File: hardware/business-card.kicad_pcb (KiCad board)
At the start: 2 copper layers, 55.5 x 89.5 mm, 91 parts, among them J1 Connector, USB-TYPE-C-16P, U1 MAX7219EWG+T, U2 AMS1117, U3 ESP32-C3FH4, X1 40MHz, 15pF

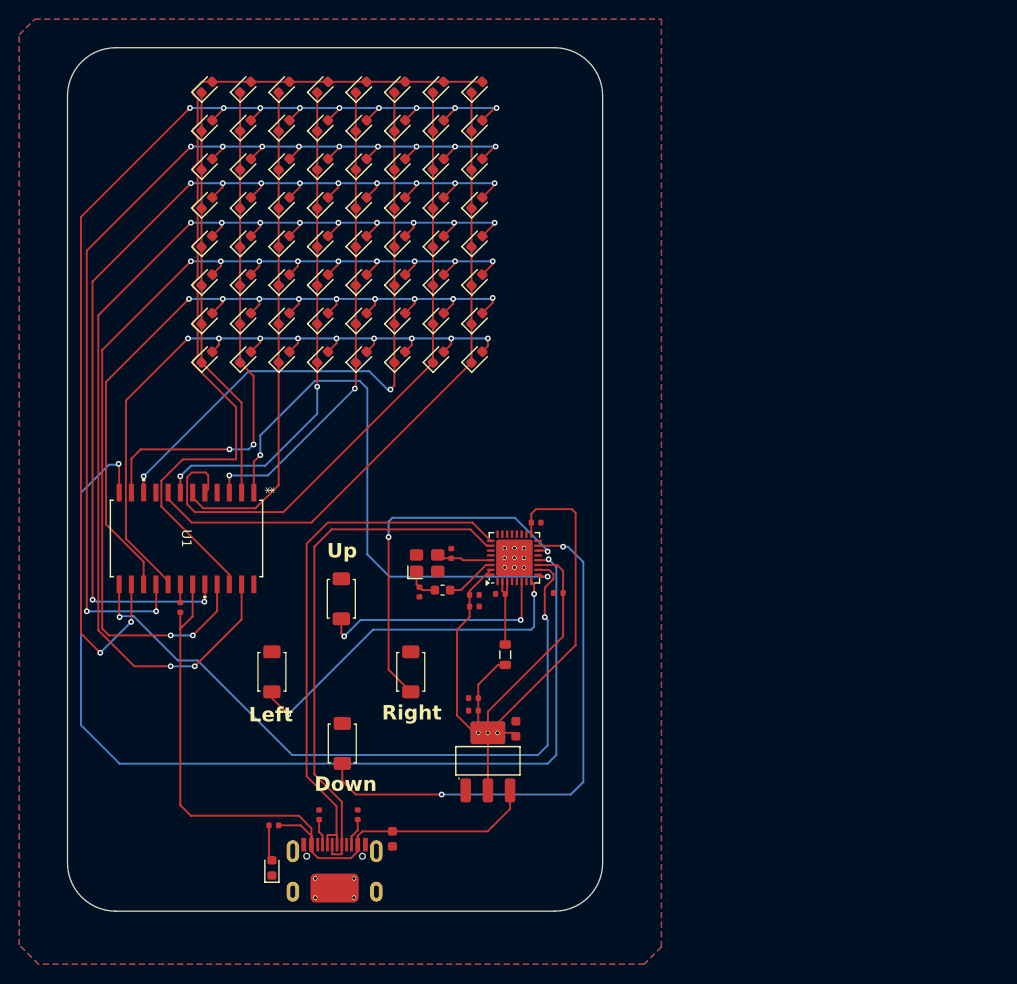
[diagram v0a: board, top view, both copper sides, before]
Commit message: Add Kicad project to hardware
Updated the hardware directory to hold the entire kicad project. Now the
pcb can be developed on multiple kicad instances and maintained in git.
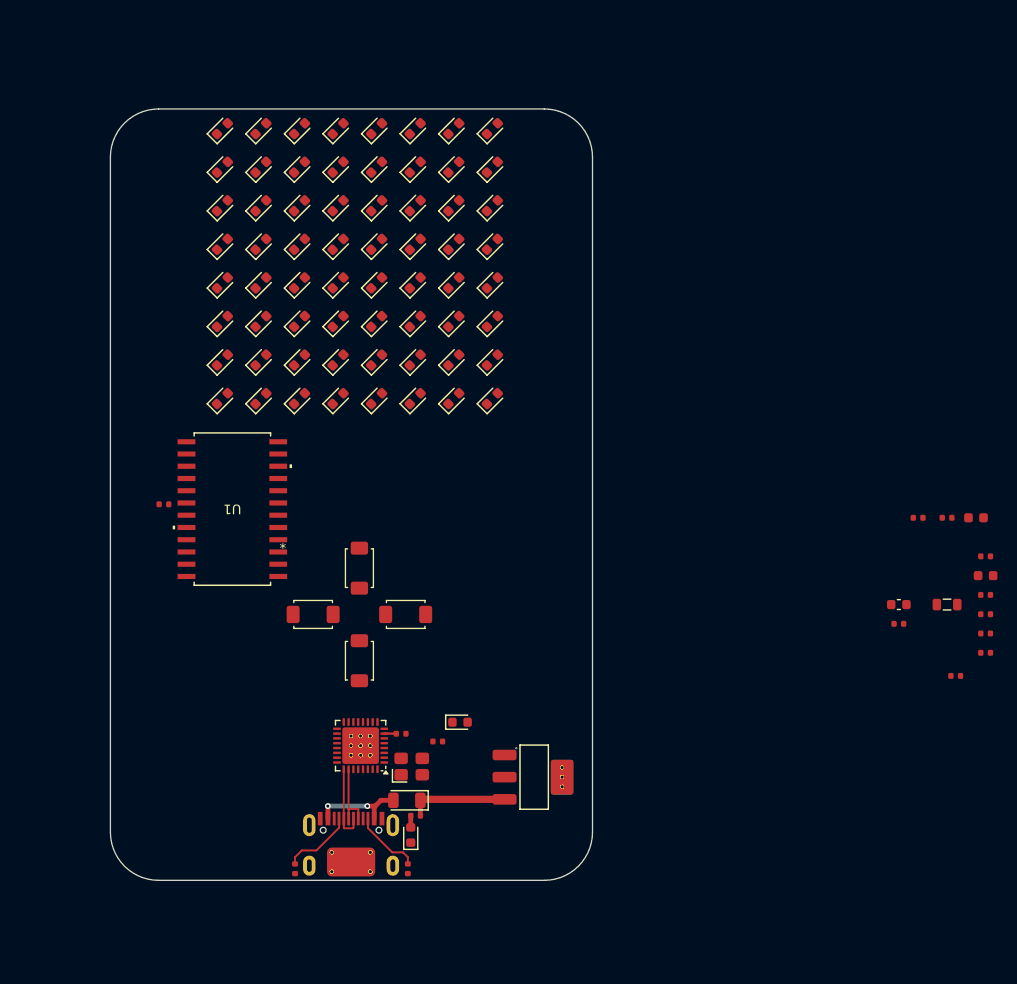
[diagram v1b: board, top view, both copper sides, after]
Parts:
- added D66: Yellow, PCM_JLCPCB:D_0603, F.Cu at (156.6, 114.4)
- added D67: SMF6.5A, PCM_JLCPCB:D_SOD-123FL, F.Cu at (151.1, 122.5)
- added R5: 1kΩ, PCM_JLCPCB:R_0402, F.Cu at (154.3, 116.4)
- added R6: 10kΩ, PCM_JLCPCB:R_0402, F.Cu at (150.5, 115.6)
- moved C1 69.1 mm to (210.1, 93.2), turned to 0 degrees
- moved C7 54.2 mm to (211.1, 101.2), turned to 0 degrees
- moved C10 53.8 mm to (208.0, 109.6), turned to 0 degrees
- moved C9 53.2 mm to (211.1, 105.2)
- moved C6 53.0 mm to (207.1, 93.2), turned to 0 degrees
- moved C4 53.0 mm to (211.1, 103.2)
- moved C2 51.2 mm to (211.1, 99.2), turned to 0 degrees
- moved C8 50.5 mm to (211.1, 97.2), turned to 0 degrees
- moved C11 49.8 mm to (202.1, 104.2), turned to 0 degrees
- moved C3 48.5 mm to (211.1, 107.2)
- moved L2 47.3 mm to (202.1, 102.2), turned to 0 degrees
- moved L1 46.1 mm to (207.1, 102.2), turned to 0 degrees
- moved C5 38.1 mm to (204.1, 93.2), turned to 0 degrees
- moved U3 25.2 mm to (146.3, 116.8), turned to 180 degrees
- moved X1 21.2 mm to (151.6, 119.0)
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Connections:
- J1 pad A9B4: VBUS -> Net-(D67-Pad2)
- J1 pad B9A4: VBUS -> Net-(D67-Pad2)
- R2 pad 2: Net-(R2-Pad2) -> GND
- U3 pad 7: unconnected-(U3-CHIP_EN-Pad7) -> Net-(U3-CHIP_EN)
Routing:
- net /R2: track 116.7 -> 0.00 mm, vias 11 -> 0
- net /R5: track 114.6 -> 0.00 mm, vias 11 -> 0
- net /R3: track 108.8 -> 0.00 mm, vias 11 -> 0
- net /R4: track 108.3 -> 0.00 mm, vias 11 -> 0
- net /GPIO6: track 105.4 -> 0.00 mm, vias 2 -> 0
- net /R6: track 103.6 -> 0.00 mm, vias 11 -> 0
- net /R1: track 95.5 -> 0.00 mm
- net +3.3V: track 95.2 -> 0.00 mm
- net /R7: track 81.5 -> 0.00 mm, vias 9 -> 0
- net /R8: track 75.0 -> 0.00 mm, vias 9 -> 0
- net /GPIO5: track 74.3 -> 0.00 mm, vias 2 -> 0
- net /C8: track 68.0 -> 0.00 mm
- net /C7: track 67.5 -> 0.00 mm
- net /C6: track 63.6 -> 0.00 mm, vias 2 -> 0
- net VBUS: track 72.7 -> 10.4 mm
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- removed copper zone on B.Cu, net GND
- removed copper zone on F.Cu, net GND
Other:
- board size 55.5 x 89.5 mm -> 50 x 80 mm
- board text removed: "Down"
- board text removed: "Jon Mahoney PCB Business Card Prototype"
- board text removed: "Left"
- board text removed: "Right"
- board text removed: "Up"

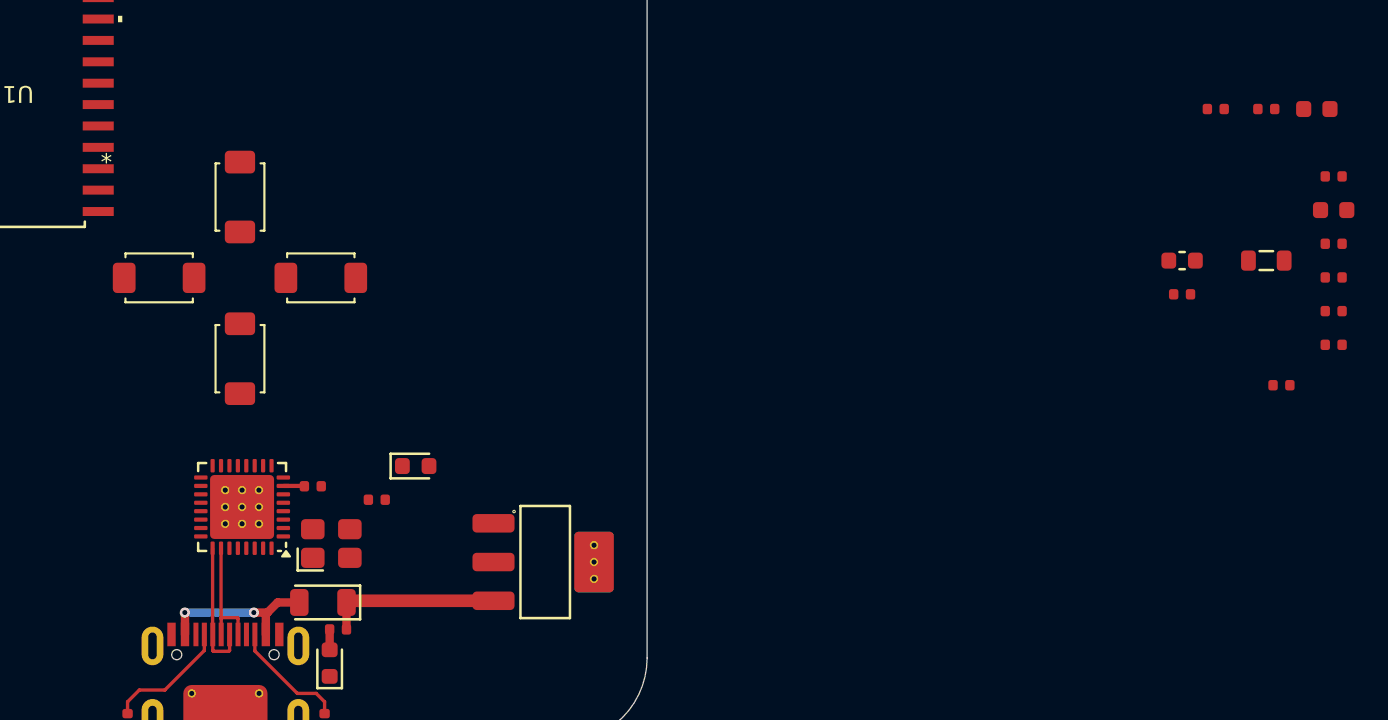
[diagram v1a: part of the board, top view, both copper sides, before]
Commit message: Updates to pcb working towards 0.2.0
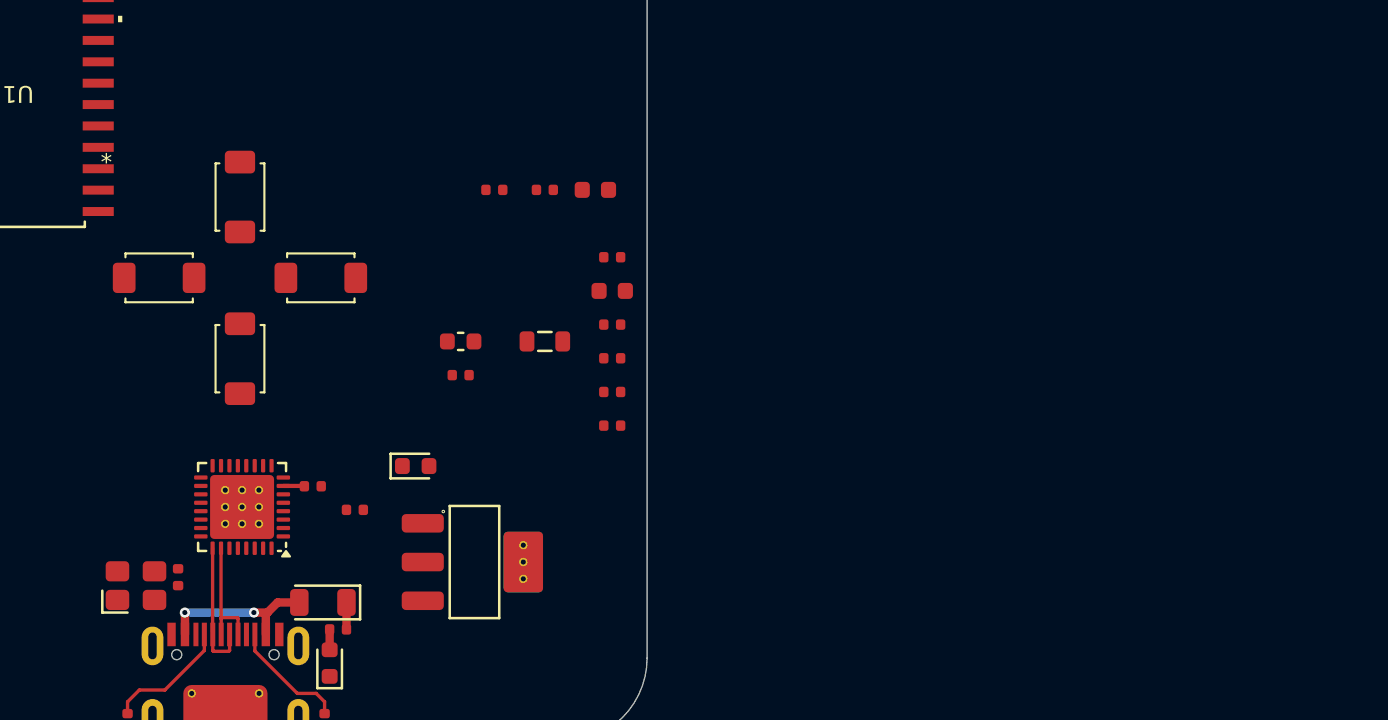
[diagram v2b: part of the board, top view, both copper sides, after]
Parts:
- moved C10 66.5 mm to (142.5, 121.0), turned to -90 degrees
- moved C1 43.1 mm to (167.3, 98.0)
- moved C11 43.1 mm to (159.3, 109.0)
- moved C2 43.1 mm to (168.3, 104.0)
- moved C3 43.1 mm to (168.3, 112.0)
- moved C4 43.1 mm to (168.3, 108.0)
- moved C5 43.1 mm to (161.3, 98.0)
- moved C6 43.1 mm to (164.3, 98.0)
- moved C7 43.1 mm to (168.3, 106.0)
- moved C8 43.1 mm to (168.3, 102.0)
- moved C9 43.1 mm to (168.3, 110.0)
- moved L1 43.1 mm to (164.3, 107.0)
- moved L2 43.1 mm to (159.3, 107.0)
- moved X1 11.9 mm to (140.0, 121.5)
- moved U2 4.20 mm to (160.0, 120.1)
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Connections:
- C5 pad 2: Net-(C5-Pad2) -> GND
- C6 pad 2: Net-(C6-Pad2) -> GND
- U3 pad 33: Net-(U3-GND) -> GND
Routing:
- net VBUS: track 10.4 -> 1.60 mm
